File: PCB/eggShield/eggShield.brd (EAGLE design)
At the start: 51.3 x 53.3 mm, 54 parts, among them J2 AVR_SPI_PRG_6NS, U1 V_REG_LDOSMD, U2 V_REG_LDOSMD, U3 MCP42XXX

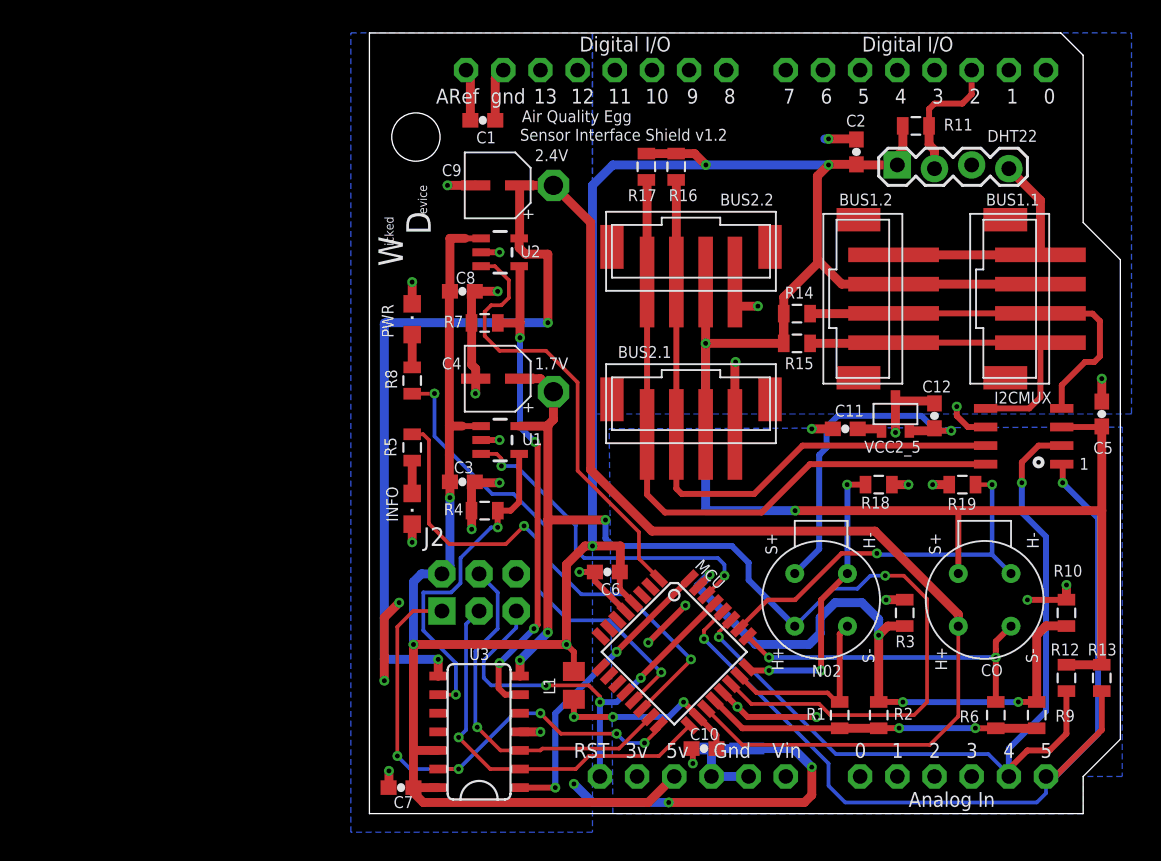
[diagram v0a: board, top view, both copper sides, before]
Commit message: added barrel jack to shield for 7-15V external power to NAnode
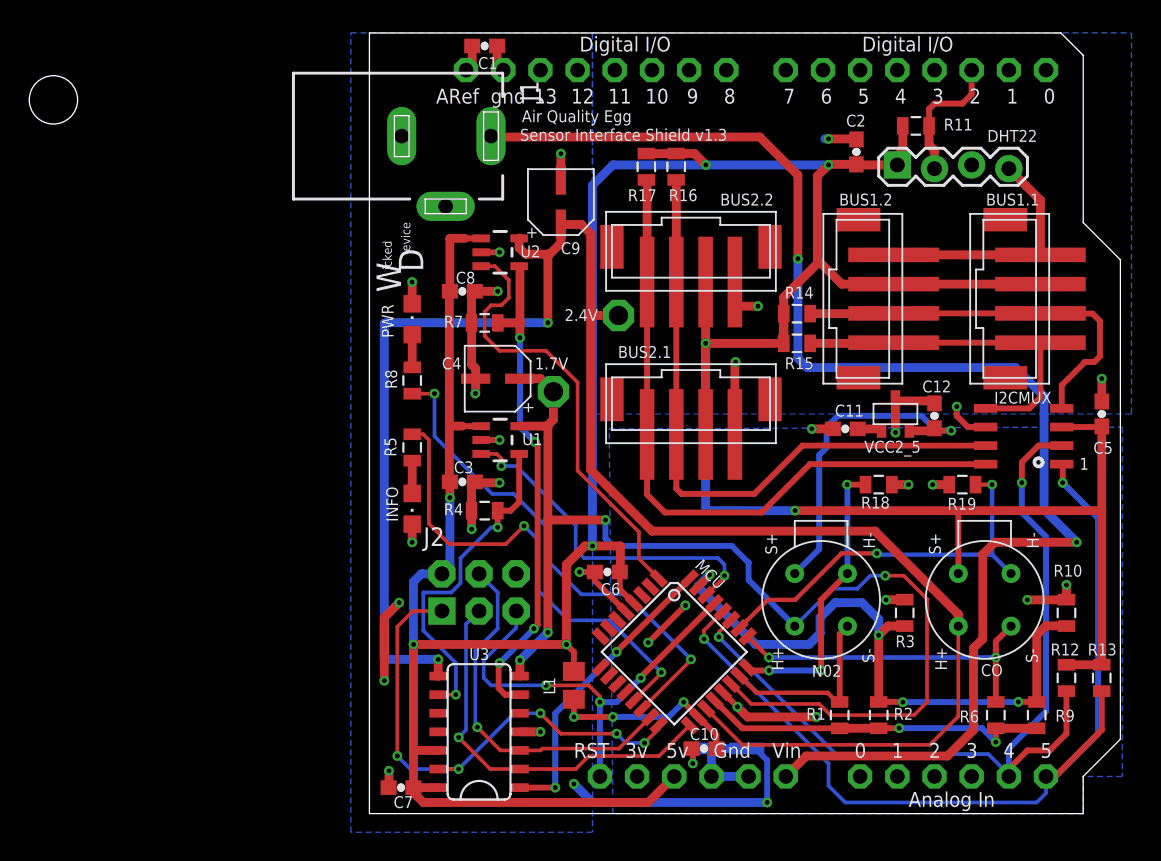
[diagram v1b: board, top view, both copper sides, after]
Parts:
- added J1: DCJ0202, con-jack:DCJ0202
- moved JP3 24.9 mm to (-21.6, 48.8)
- moved TP2 9.94 mm to (17.0, 34.0)
- moved C1 5.08 mm to (7.87, 52.5)
- moved C9 4.47 mm to (13.1, 41.8), turned to 0 degrees
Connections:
- net GND: now also J1.3
- net VIN: now also J1.1
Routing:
- net VIN: track 0.00 -> 96.5 mm, vias 0 -> 2
- net GND: track 94.7 -> 87.2 mm, vias 22 -> 21
- net CO_HEATER_V: track 128.2 -> 124.7 mm
- net N$4: track 3.55 -> 1.82 mm
- net /R1_SEL: track 22.8 -> 24.2 mm
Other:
- board text added: "Sensor Interface Shield v1.3"
- board text removed: "Sensor Interface Shield v1.2"

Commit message: added silk screen to barrel jack to make voltage input range and polarity clear
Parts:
- renumbered J1 to 7-12VDC
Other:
- board text added: "center (+)"
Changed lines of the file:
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@@
 <text x="10.287" y="45.974" size="0.8128" layer="21" font="vector">Sensor Interface Shield v1.3</text>
 <circle x="45.72" y="24.003" radius="0.283978125" width="0.254" layer="21"/>
+<text x="0.4445" y="50.9905" size="0.6096" layer="21" font="vector">center (+)</text>
 </plain>
 <attributes>
@@
 </element>
 <element name="J2" library="SparkFun" package="2X3-NS" value="AVR_SPI_PRG_6NS" x="7.493" y="15.113"/>
-<element name="J1" library="con-jack" package="DCJ0202" value="DCJ0202" x="5.207" y="46.2915" rot="R270"/>
+<element name="7-12VDC" library="con-jack" package="DCJ0202" value="DCJ0202" x="5.207" y="46.2915" smashed="yes" rot="R270">
+<attribute name="NAME" x="1.5875" y="52.0065" size="0.6096" layer="25" font="vector"/>
+<attribute name="VALUE" x="-4.953" y="51.3715" size="1.27" layer="27"/>
+</element>
 </elements>
 <signals>
@@
 <wire x1="27.178" y1="3.648" x2="27.178" y2="0.762" width="0.4064" layer="16"/>
 <wire x1="27.178" y1="0.762" x2="15.24" y2="0.762" width="0.6096" layer="16"/>
-<contactref element="J1" pad="3"/>
+<contactref element="7-12VDC" pad="3"/>
 </signal>
 <signal name="CO_RH-">
@@
 <signal name="VIN">
 <contactref element="U$7" pad="VIN"/>
-<contactref element="J1" pad="1"/>
+<contactref element="7-12VDC" pad="1"/>
 <wire x1="28.448" y1="2.54" x2="29.845" y2="3.937" width="0.6096" layer="1"/>
 <wire x1="29.845" y1="3.937" x2="39.497" y2="3.937" width="0.6096" layer="1"/>

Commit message: deleted registration hole that was sitting out in the middle of nowhere
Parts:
- removed JP3: STAND-OFF, SparkFun:STAND-OFF
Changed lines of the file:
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@@
 <attribute name="NAME" x="20.632" y="31.946" size="0.8128" layer="25" font="vector" rot="R180"/>
 </element>
-<element name="JP3" library="SparkFun" package="STAND-OFF" value="STAND-OFF" x="-21.59" y="48.768" rot="MR0"/>
 <element name="R14" library="SparkFun" package="0805" value="1.8kOhm" x="29.21" y="34.163" smashed="yes" rot="R180">
 <attribute name="NAME" x="30.353" y="36.0045" size="0.8128" layer="25" font="vector" rot="R180"/>

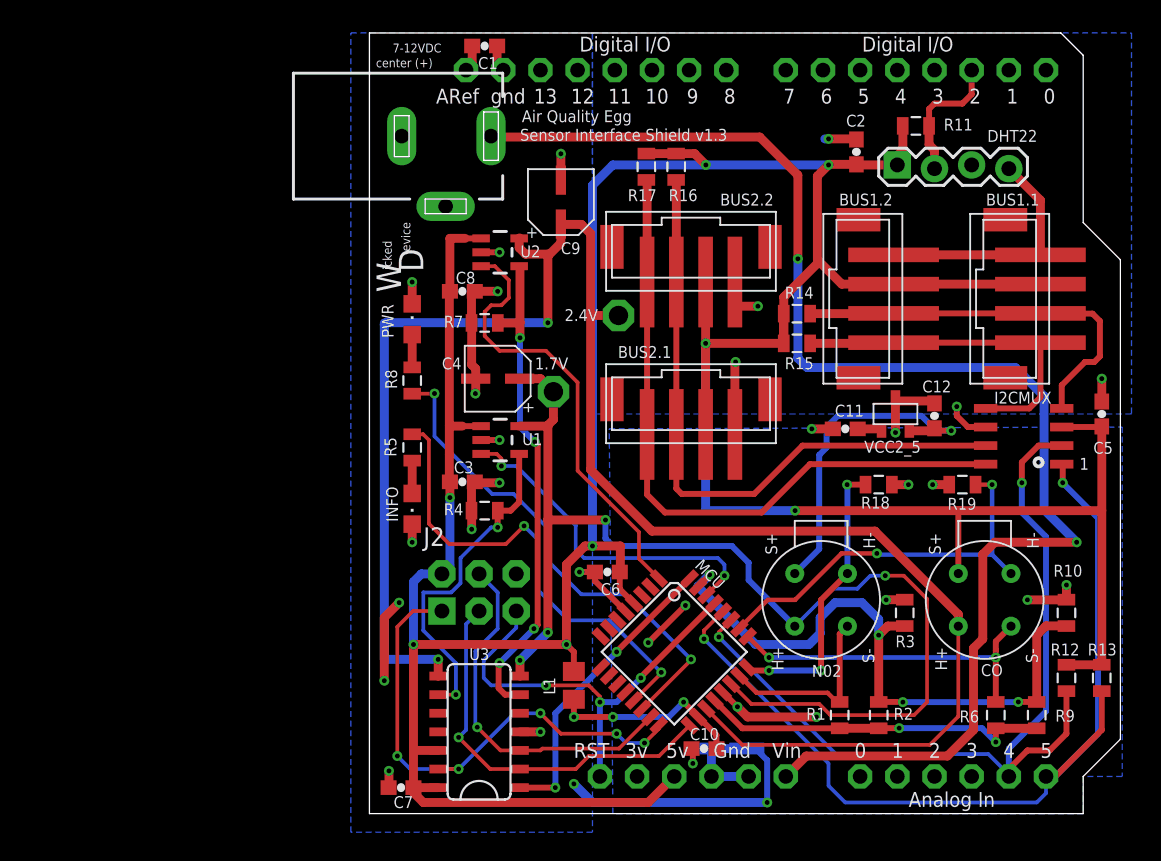
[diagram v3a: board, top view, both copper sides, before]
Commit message: routed DHT22 to A3
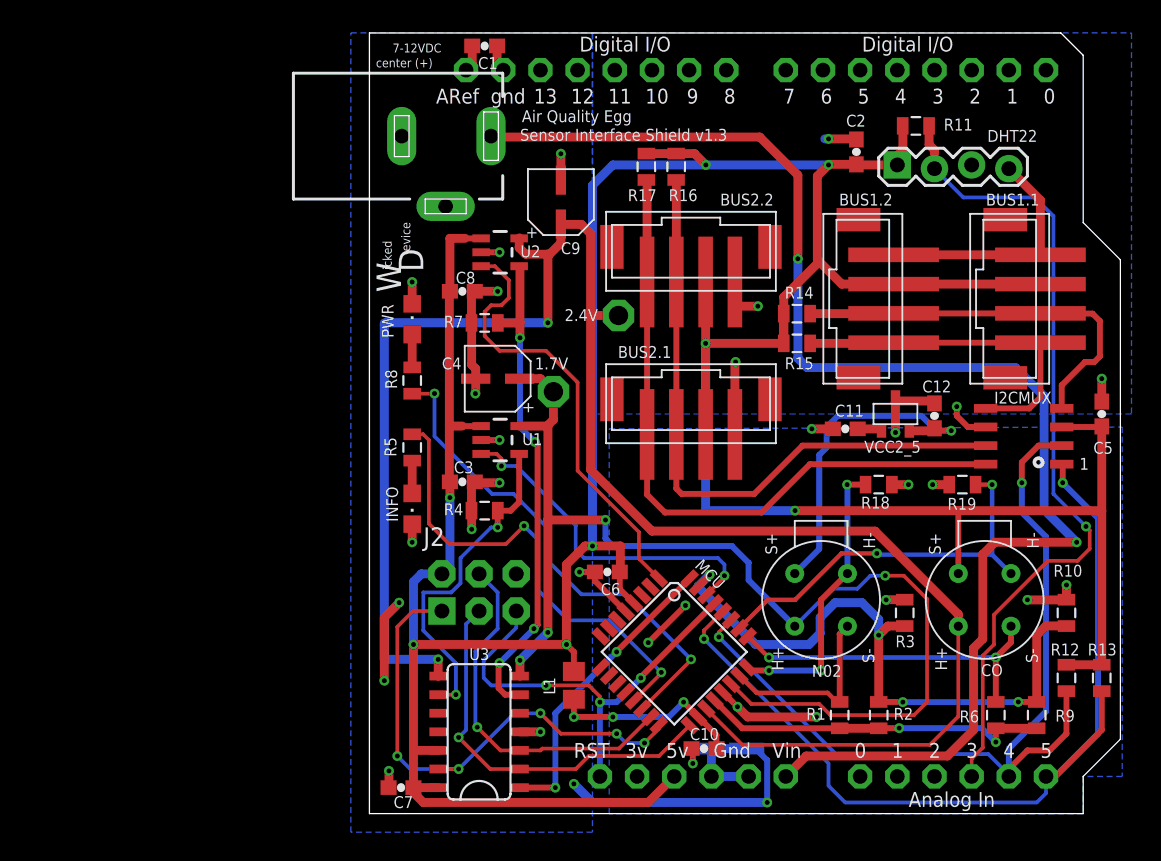
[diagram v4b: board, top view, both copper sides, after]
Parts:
- R1: value (none) -> 2.2kOhm
- R10: value (none) -> 680kOhm
- R18, R19: value (none) -> 68Ohm
- R2: value (none) -> 22kOhm
- R3: value (none) -> 220kOhm
- R4: value 1.8MOhm -> 120kOhm
- R6, R9: value (none) -> 68kOhm
- R7: value 750kOhm -> 56kOhm
- R8: value 470ohm -> 270ohm
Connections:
- net DHT22_IO: now also U$7.A3; no longer U$7.D2
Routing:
- net DHT22_IO: track 9.21 -> 56.4 mm, vias 0 -> 1
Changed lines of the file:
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@@
 <layer number="20" name="Dimension" color="15" fill="1" visible="yes" active="yes"/>
 <layer number="21" name="tPlace" color="7" fill="1" visible="yes" active="yes"/>
-<layer number="22" name="bPlace" color="7" fill="1" visible="yes" active="yes"/>
+<layer number="22" name="bPlace" color="7" fill="1" visible="no" active="yes"/>
 <layer number="23" name="tOrigins" color="15" fill="1" visible="yes" active="yes"/>
 <layer number="24" name="bOrigins" color="15" fill="1" visible="yes" active="yes"/>
@@
 <attribute name="NAME" x="32.258" y="10.16" size="0.8128" layer="25" font="vector" rot="R180"/>
 </element>
-<element name="R1" library="SparkFun" package="0805" value="" x="32.131" y="6.731" smashed="yes" rot="R90">
+<element name="R1" library="SparkFun" package="0805" value="2.2kOhm" x="32.131" y="6.731" smashed="yes" rot="R90">
 <attribute name="NAME" x="29.845" y="6.4135" size="0.8128" layer="25" font="vector"/>
 <attribute name="VALUE" x="33.528" y="5.715" size="0.4064" layer="27" rot="R90"/>
 </element>
-<element name="R4" library="SparkFun" package="0805" value="1.8MOhm" x="7.874" y="20.701" smashed="yes">
+<element name="R4" library="SparkFun" package="0805" value="120kOhm" x="7.874" y="20.701" smashed="yes">
 <attribute name="NAME" x="5.08" y="20.3835" size="0.8128" layer="25" font="vector"/>
 <attribute name="VALUE" x="6.858" y="19.304" size="0.4064" layer="27"/>
@@
 <attribute name="NAME" x="11.811" y="25.9939" size="0.8128" layer="25" font="vector" rot="R180"/>
 </element>
-<element name="R2" library="SparkFun" package="0805" value="" x="34.798" y="6.731" smashed="yes" rot="R270">
+<element name="R2" library="SparkFun" package="0805" value="22kOhm" x="34.798" y="6.731" smashed="yes" rot="R270">
 <attribute name="NAME" x="35.814" y="6.4135" size="0.8128" layer="25" font="vector"/>
 <attribute name="VALUE" x="33.401" y="7.747" size="0.4064" layer="27" rot="R270"/>
 </element>
-<element name="R3" library="SparkFun" package="0805" value="" x="36.576" y="13.716" smashed="yes" rot="R270">
+<element name="R3" library="SparkFun" package="0805" value="220kOhm" x="36.576" y="13.716" smashed="yes" rot="R270">
 <attribute name="NAME" x="35.941" y="11.3665" size="0.8128" layer="25" font="vector"/>
 <attribute name="VALUE" x="35.179" y="14.732" size="0.4064" layer="27" rot="R270"/>
@@
 <attribute name="VALUE" x="10.881" y="44.533" size="0.3048" layer="27"/>
 </element>
-<element name="R7" library="SparkFun" package="0805" value="750kOhm" x="7.874" y="33.528" smashed="yes">
+<element name="R7" library="SparkFun" package="0805" value="56kOhm" x="7.874" y="33.528" smashed="yes">
 <attribute name="NAME" x="5.08" y="33.2105" size="0.8128" layer="25" font="vector"/>
 <attribute name="VALUE" x="6.858" y="32.131" size="0.4064" layer="27"/>
@@
 <attribute name="NAME" x="41.783" y="9.398" size="0.8128" layer="25" font="vector"/>
 </element>
-<element name="R6" library="SparkFun" package="0805" value="" x="42.799" y="6.731" smashed="yes" rot="R90">
+<element name="R6" library="SparkFun" package="0805" value="68kOhm" x="42.799" y="6.731" smashed="yes" rot="R90">
 <attribute name="NAME" x="41.656" y="7.0485" size="0.8128" layer="25" font="vector" rot="R180"/>
 <attribute name="VALUE" x="44.196" y="5.715" size="0.4064" layer="27" rot="R90"/>
 </element>
-<element name="R9" library="SparkFun" package="0805" value="" x="45.593" y="6.731" smashed="yes" rot="R270">
+<element name="R9" library="SparkFun" package="0805" value="68kOhm" x="45.593" y="6.731" smashed="yes" rot="R270">
 <attribute name="NAME" x="46.863" y="6.2865" size="0.8128" layer="25" font="vector"/>
 <attribute name="VALUE" x="44.196" y="7.747" size="0.4064" layer="27" rot="R270"/>
 </element>
-<element name="R10" library="SparkFun" package="0805" value="" x="47.625" y="13.716" smashed="yes" rot="R270">
+<element name="R10" library="SparkFun" package="0805" value="680kOhm" x="47.625" y="13.716" smashed="yes" rot="R270">
 <attribute name="NAME" x="46.736" y="16.1925" size="0.8128" layer="25" font="vector"/>
 <attribute name="VALUE" x="46.228" y="14.732" size="0.4064" layer="27" rot="R270"/>
@@
 <attribute name="NAME" x="8.1915" y="11.303" size="0.8128" layer="25" font="vector" rot="R180"/>
 </element>
-<element name="R18" library="SparkFun" package="0805" value="" x="34.798" y="22.479" smashed="yes" rot="R180">
+<element name="R18" library="SparkFun" package="0805" value="68Ohm" x="34.798" y="22.479" smashed="yes" rot="R180">
 <attribute name="NAME" x="35.56" y="21.6535" size="0.8128" layer="25" font="vector" rot="R180"/>
 <attribute name="VALUE" x="35.814" y="23.876" size="0.4064" layer="27" rot="R180"/>
 </element>
-<element name="R19" library="SparkFun" package="0805" value="" x="40.513" y="22.479" smashed="yes">
+<element name="R19" library="SparkFun" package="0805" value="68Ohm" x="40.513" y="22.479" smashed="yes">
 <attribute name="NAME" x="39.497" y="20.7645" size="0.8128" layer="25" font="vector"/>
 <attribute name="VALUE" x="39.497" y="21.082" size="0.4064" layer="27"/>
@@
 <attribute name="VALUE" x="5.461" y="32.512" size="1.27" layer="27" rot="R90"/>
 </element>
-<element name="R8" library="SparkFun" package="0805" value="470ohm" x="2.921" y="29.591" smashed="yes" rot="R270">
+<element name="R8" library="SparkFun" package="0805" value="270ohm" x="2.921" y="29.591" smashed="yes" rot="R270">
 <attribute name="NAME" x="1.0795" y="30.353" size="0.8128" layer="25" font="vector" rot="R270"/>
 <attribute name="VALUE" x="1.524" y="30.607" size="0.4064" layer="27" rot="R270"/>
@@
 <contactref element="CO" pad="FIGV+/E2VSIG"/>
 <contactref element="R6" pad="2"/>
-<wire x1="43.837" y1="12.805" x2="42.799" y2="11.767" width="0.4064" layer="1"/>
-<wire x1="42.799" y1="11.767" x2="42.799" y2="11.176" width="0.4064" layer="1"/>
 <contactref element="MCU" pad="25"/>
-<wire x1="42.799" y1="11.176" x2="42.799" y2="10.668" width="0.4064" layer="1"/>
 <wire x1="42.799" y1="10.668" x2="42.799" y2="7.631" width="0.4064" layer="1"/>
 <wire x1="25.843225" y1="12.104425" x2="27.27965" y2="10.668" width="0.3048" layer="1"/>
@@
 <wire x1="27.305" y1="10.668" x2="42.799" y2="10.668" width="0.3048" layer="16"/>
 <via x="42.799" y="10.668" extent="1-16" drill="0.3302"/>
+<wire x1="42.799" y1="10.668" x2="43.837" y2="11.706" width="0.4064" layer="1"/>
+<wire x1="43.837" y1="11.706" x2="43.837" y2="12.805" width="0.4064" layer="1"/>
 </signal>
 <signal name="SDA">
@@
 </signal>
 <signal name="DHT22_IO">
-<contactref element="U$7" pad="D2"/>
 <contactref element="DHT22" pad="DATA"/>
 <contactref element="R11" pad="2"/>
@@
 <wire x1="38.238" y1="45.709" x2="38.608" y2="45.339" width="0.6096" layer="1"/>
 <wire x1="38.608" y1="45.339" x2="38.608" y2="44.069" width="0.6096" layer="1"/>
-<wire x1="38.238" y1="46.99" x2="38.238" y2="48.144" width="0.4064" layer="1"/>
-<wire x1="38.238" y1="48.144" x2="38.608" y2="48.514" width="0.4064" layer="1"/>
-<wire x1="38.608" y1="48.514" x2="40.513" y2="48.514" width="0.4064" layer="1"/>
-<wire x1="40.513" y1="48.514" x2="41.148" y2="49.149" width="0.4064" layer="1"/>
-<wire x1="41.148" y1="49.149" x2="41.148" y2="50.8" width="0.4064" layer="1"/>
+<contactref element="U$7" pad="A3"/>
+<wire x1="41.148" y1="2.54" x2="41.148" y2="3.7465" width="0.254" layer="1"/>
+<wire x1="41.148" y1="3.7465" x2="41.91" y2="4.5085" width="0.254" layer="1"/>
+<wire x1="41.91" y1="4.5085" x2="41.91" y2="10.795" width="0.254" layer="1"/>
+<wire x1="41.91" y1="10.795" x2="42.672" y2="11.557" width="0.254" layer="1"/>
+<wire x1="42.672" y1="11.557" x2="42.672" y2="13.589" width="0.254" layer="1"/>
+<wire x1="42.672" y1="13.589" x2="46.355" y2="17.272" width="0.254" layer="1"/>
+<wire x1="46.355" y1="17.272" x2="48.387" y2="17.272" width="0.254" layer="1"/>
+<wire x1="48.387" y1="17.272" x2="49.2125" y2="18.0975" width="0.254" layer="1"/>
+<wire x1="49.2125" y1="18.0975" x2="49.2125" y2="19.3675" width="0.254" layer="1"/>
+<wire x1="49.2125" y1="19.3675" x2="48.9585" y2="19.6215" width="0.254" layer="1"/>
+<via x="48.9585" y="19.6215" extent="1-16" drill="0.3302"/>
+<wire x1="48.9585" y1="19.6215" x2="46.736" y2="21.844" width="0.254" layer="16"/>
+<wire x1="46.736" y1="21.844" x2="46.736" y2="40.8305" width="0.254" layer="16"/>
+<wire x1="46.736" y1="40.8305" x2="45.466" y2="42.1005" width="0.254" layer="16"/>
+<wire x1="45.466" y1="42.1005" x2="40.5765" y2="42.1005" width="0.254" layer="16"/>
+<wire x1="40.5765" y1="42.1005" x2="38.608" y2="44.069" width="0.254" layer="16"/>
 </signal>
 <signal name="SCK">
@@
 <vertex x="48.768" y="2.54"/>
 <vertex x="48.768" y="0"/>
-<vertex x="16.637" y="0"/>
+<vertex x="16.383" y="0"/>
 </polygon>
 <wire x1="47.625" y1="15.621" x2="47.625" y2="14.605" width="0.4064" layer="1"/>

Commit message: fixed 2.5v regulator bug
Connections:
- removed net N$2: C11.1, VCC2_5.1
- net 5V: now also C11.1, VCC2_5.1
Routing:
- net 5V: track 257.8 -> 272.5 mm, vias 8 -> 9
- net N$2: track 1.68 -> 0.00 mm
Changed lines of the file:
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@@
 <wire x1="22.971" y1="20.701" x2="22.971" y2="32.131" width="0.6096" layer="16"/>
 <via x="22.971" y="32.131" extent="1-16" drill="0.3302"/>
+<contactref element="VCC2_5" pad="1"/>
+<contactref element="C11" pad="1"/>
+<wire x1="33.362" y1="26.289" x2="34.857" y2="26.289" width="0.6096" layer="1"/>
+<wire x1="34.857" y1="26.289" x2="34.991" y2="26.155" width="0.6096" layer="1"/>
+<wire x1="29.083" y1="20.701" x2="29.083" y2="27.051" width="0.6096" layer="16"/>
+<wire x1="29.083" y1="27.051" x2="30.226" y2="28.194" width="0.6096" layer="16"/>
+<wire x1="30.226" y1="28.194" x2="33.3375" y2="28.194" width="0.6096" layer="16"/>
+<via x="33.3375" y="28.194" extent="1-16" drill="0.3302"/>
+<wire x1="33.3375" y1="28.194" x2="33.362" y2="28.1695" width="0.6096" layer="1"/>
+<wire x1="33.362" y1="28.1695" x2="33.362" y2="26.289" width="0.6096" layer="1"/>
 </signal>
 <signal name="MOSI_B">
@@
 <wire x1="2.921" y1="32.732" x2="2.921" y2="30.491" width="0.6096" layer="1"/>
 </signal>
-<signal name="N$2">
-<contactref element="VCC2_5" pad="1"/>
-<contactref element="C11" pad="1"/>
-<wire x1="33.362" y1="26.289" x2="34.857" y2="26.289" width="0.6096" layer="1"/>
-<wire x1="34.857" y1="26.289" x2="34.991" y2="26.155" width="0.6096" layer="1"/>
-</signal>
 <signal name="VIN">
